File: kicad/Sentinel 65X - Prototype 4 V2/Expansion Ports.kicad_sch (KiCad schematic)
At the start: 15 parts, among them J4 Conn_02x14_Odd_Even, J5 2x32 2.54mm Card Edge Connect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

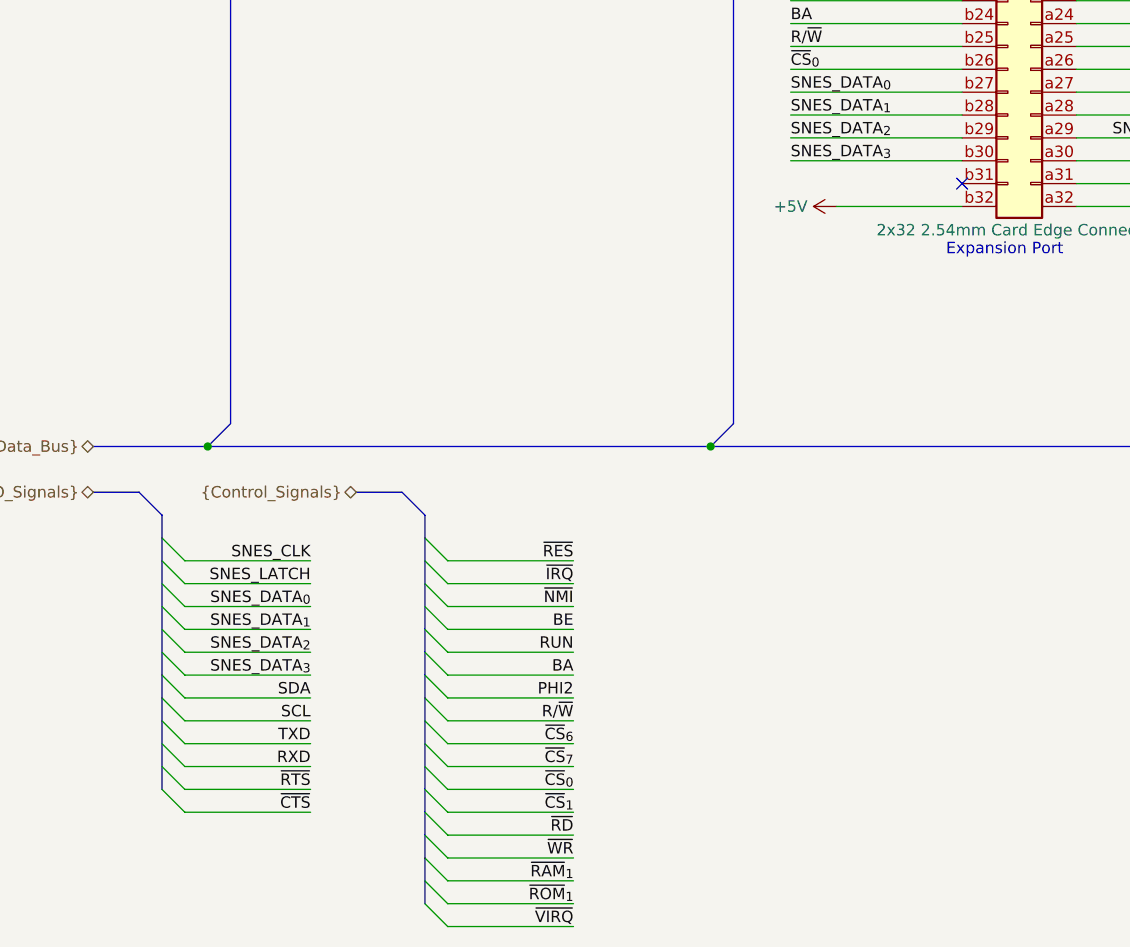
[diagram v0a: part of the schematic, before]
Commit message: Updated prototype 4V2 schematic
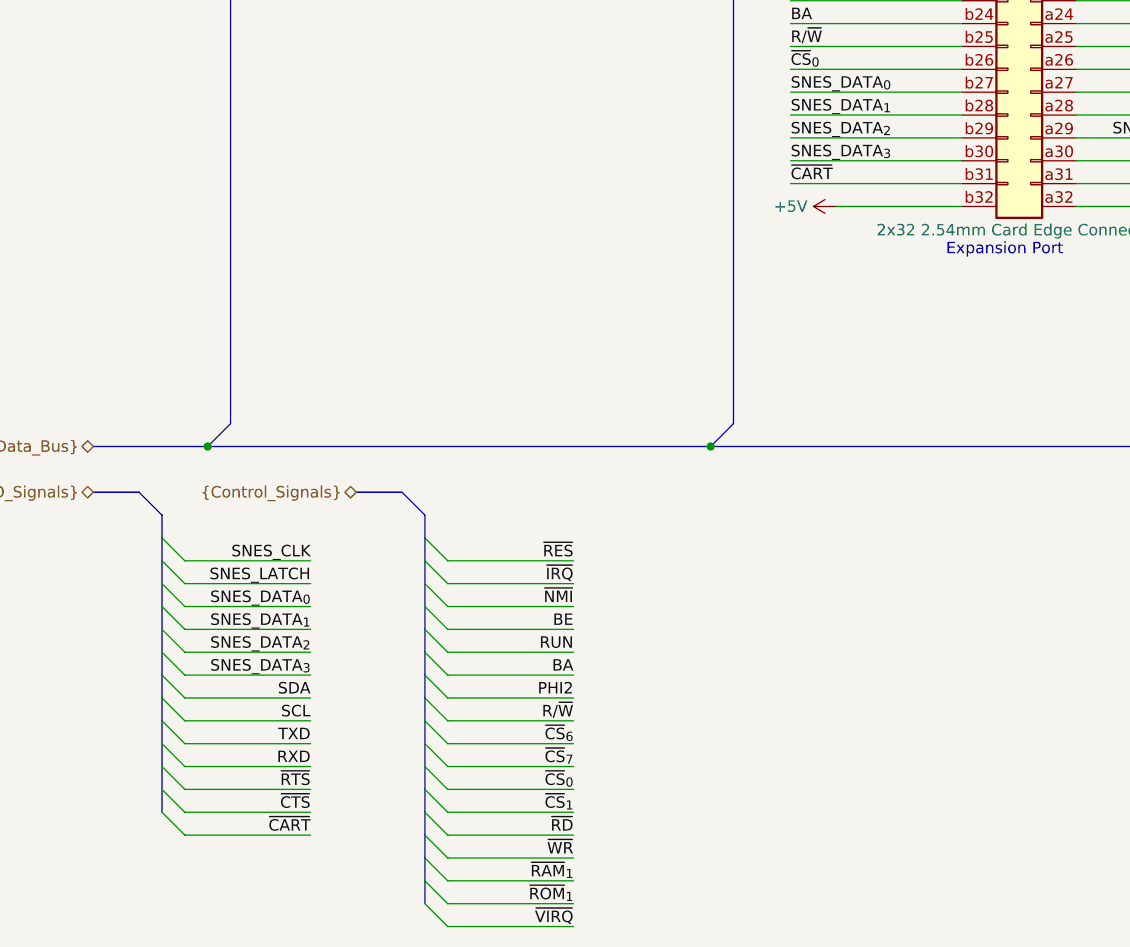
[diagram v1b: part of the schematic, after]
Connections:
- net ~{CART}: now reaches J5.b31 (Pin_b31)
- no-connect marks 7 -> 6
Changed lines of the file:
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@@
 	)
 	(no_connect
-		(at 123.19 105.41)
-	)
-	(no_connect
 		(at 229.87 129.54)
 	)
@@
 	)
 	(bus_entry
+		(at 34.29 175.26)
+		(size 2.54 2.54)
+		(stroke
+			(width 0)
+			(type default)
+		)
+	)
+	(bus_entry
 		(at 63.5 182.88)
 		(size 2.54 2.54)
@@
 	(wire
 		(pts
+			(xy 36.83 177.8) (xy 50.8 177.8)
+		)
+		(stroke
+			(width 0)
+			(type default)
+		)
+	)
+	(wire
+		(pts
 			(xy 74.93 55.88) (xy 86.36 55.88)
 		)
@@
 	(wire
 		(pts
+			(xy 104.14 105.41) (xy 123.19 105.41)
+		)
+		(stroke
+			(width 0)
+			(type default)
+		)
+	)
+	(wire
+		(pts
 			(xy 66.04 157.48) (xy 80.01 157.48)
 		)
@@
 		)
 	)
+	(bus
+		(pts
+			(xy 34.29 172.72) (xy 34.29 175.26)
+		)
+		(stroke
+			(width 0)
+			(type default)
+		)
+	)
 	(wire
 		(pts
@@
 		)
 	)
+	(label "~{CART}"
+		(at 50.8 177.8 180)
+		(fields_autoplaced yes)
+		(effects
+			(font
+				(size 1.27 1.27)
+			)
+			(justify right bottom)
+		)
+	)
 	(label "BE"
 		(at 80.01 154.94 180)
@@
 		)
 	)
+	(label "~{CART}"
+		(at 104.14 105.41 0)
+		(fields_autoplaced yes)
+		(effects
+			(font
+				(size 1.27 1.27)
+			)
+			(justify left bottom)
+		)
+	)
